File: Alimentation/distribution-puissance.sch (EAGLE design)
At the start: 18 parts

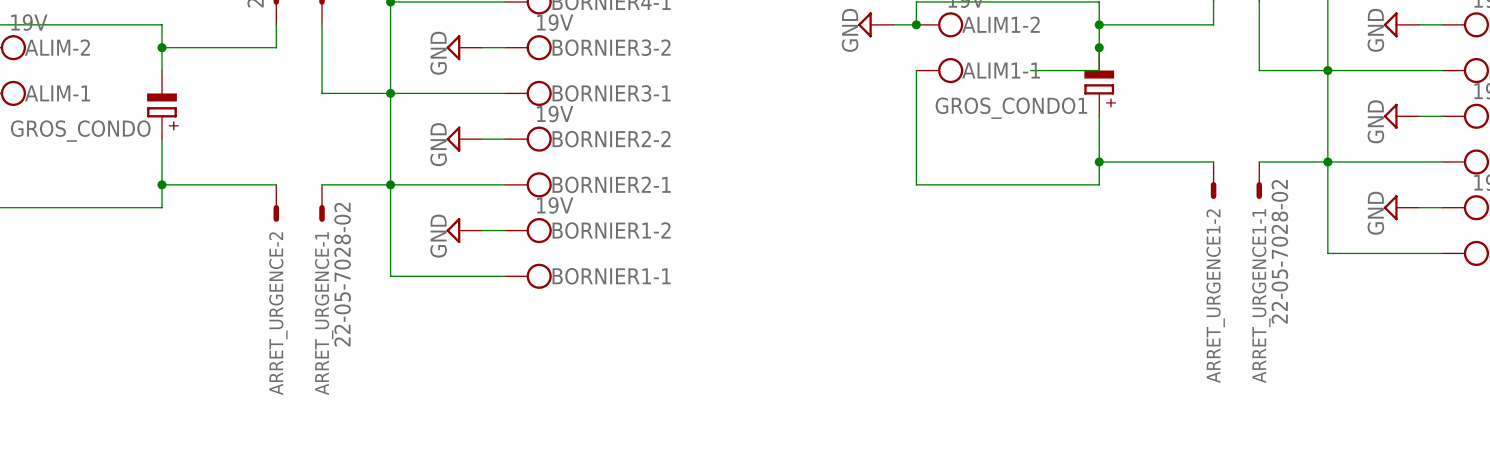
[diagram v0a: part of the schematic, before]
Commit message: utilisation de bornier pour les ARU + plus grosses pistes dans le routage + gerber files
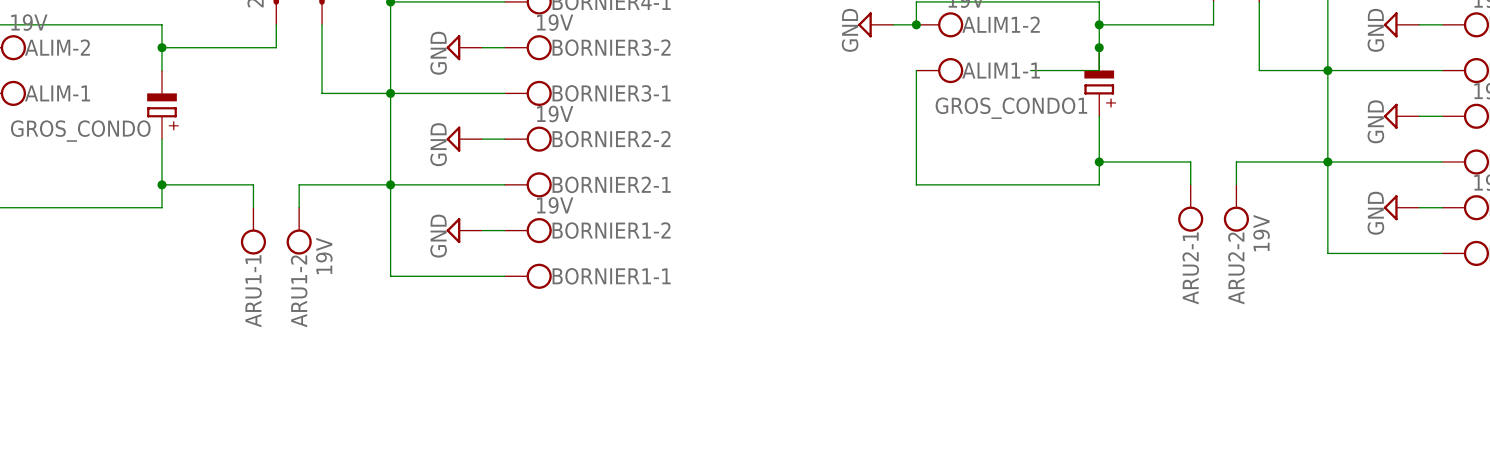
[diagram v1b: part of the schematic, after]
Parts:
- removed ARRET_URGENCE, ARRET_URGENCE1: 22-05-7028-02, con-molex:22-05-7028-02
- added ARU1, ARU2: 19V, con-wago-500:W237-102
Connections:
- net N$1: now also ARU1-2.KL; no longer ARRET_URGENCE-1.S
- net N$2: now also ARU2-2.KL; no longer ARRET_URGENCE1-1.S
- net N$3: now also ARU1-1.KL; no longer ARRET_URGENCE-2.S
- net N$4: now also ARU2-1.KL; no longer ARRET_URGENCE1-2.S
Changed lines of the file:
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@@
 <part name="FRAME1" library="frames" library_urn="urn:adsk.eagle:library:229" deviceset="A4L-LOC" device=""/>
 <part name="GROS_CONDO" library="rcl" library_urn="urn:adsk.eagle:library:334" deviceset="CPOL-EU" device="E10-22.5"/>
-<part name="ARRET_URGENCE" library="con-molex" library_urn="urn:adsk.eagle:library:165" deviceset="22-?-02" device="05-7028"/>
 <part name="VOLTMETRE" library="con-molex" library_urn="urn:adsk.eagle:library:165" deviceset="22-?-02" device="05-7028"/>
 <part name="BORNIER1" library="con-wago-500" library_urn="urn:adsk.eagle:library:195" deviceset="W237-102" device="" value="19V"/>
@@
 <part name="BATTERIE_GND6" library="supply2" library_urn="urn:adsk.eagle:library:372" deviceset="GND" device=""/>
 <part name="GROS_CONDO1" library="rcl" library_urn="urn:adsk.eagle:library:334" deviceset="CPOL-EU" device="E10-22.5"/>
-<part name="ARRET_URGENCE1" library="con-molex" library_urn="urn:adsk.eagle:library:165" deviceset="22-?-02" device="05-7028"/>
 <part name="VOLTMETRE1" library="con-molex" library_urn="urn:adsk.eagle:library:165" deviceset="22-?-02" device="05-7028"/>
 <part name="BORNIER6" library="con-wago-500" library_urn="urn:adsk.eagle:library:195" deviceset="W237-102" device="" value="19V"/>
@@
 <part name="ALIM1" library="con-wago-500" library_urn="urn:adsk.eagle:library:195" deviceset="W237-102" device="" value="19V"/>
 <part name="BATTERIE_GND12" library="supply2" library_urn="urn:adsk.eagle:library:372" deviceset="GND" device=""/>
+<part name="ARU1" library="con-wago-500" library_urn="urn:adsk.eagle:library:195" deviceset="W237-102" device="" value="19V"/>
+<part name="ARU2" library="con-wago-500" library_urn="urn:adsk.eagle:library:195" deviceset="W237-102" device="" value="19V"/>
 </parts>
 <sheets>
@@
 <instance part="FRAME1" gate="G$1" x="0" y="0"/>
 <instance part="GROS_CONDO" gate="G$1" x="35.56" y="88.9" rot="R180"/>
-<instance part="ARRET_URGENCE" gate="-1" x="53.34" y="78.74" rot="R270"/>
-<instance part="ARRET_URGENCE" gate="-2" x="48.26" y="78.74" rot="R270"/>
 <instance part="VOLTMETRE" gate="-1" x="48.26" y="101.6" rot="R90"/>
 <instance part="VOLTMETRE" gate="-2" x="53.34" y="101.6" rot="R90"/>
@@
 <instance part="BATTERIE_GND6" gate="GND" x="10.16" y="96.52" rot="R270"/>
 <instance part="GROS_CONDO1" gate="G$1" x="139.7" y="91.44" rot="R180"/>
-<instance part="ARRET_URGENCE1" gate="-1" x="157.48" y="81.28" rot="R270"/>
-<instance part="ARRET_URGENCE1" gate="-2" x="152.4" y="81.28" rot="R270"/>
 <instance part="VOLTMETRE1" gate="-1" x="152.4" y="104.14" rot="R90"/>
 <instance part="VOLTMETRE1" gate="-2" x="157.48" y="104.14" rot="R90"/>
@@
 <instance part="ALIM1" gate="-2" x="124.46" y="99.06" rot="R180"/>
 <instance part="BATTERIE_GND12" gate="GND" x="114.3" y="99.06" rot="R270"/>
+<instance part="ARU1" gate="-1" x="45.72" y="73.66" rot="R90"/>
+<instance part="ARU1" gate="-2" x="50.8" y="73.66" rot="R90"/>
+<instance part="ARU2" gate="-1" x="149.86" y="76.2" rot="R90"/>
+<instance part="ARU2" gate="-2" x="154.94" y="76.2" rot="R90"/>
 </instances>
 <busses>
@@
 <net name="N$1" class="0">
 <segment>
-<pinref part="ARRET_URGENCE" gate="-1" pin="S"/>
-<wire x1="53.34" y1="81.28" x2="60.96" y2="81.28" width="0.1524" layer="91"/>
 <wire x1="60.96" y1="81.28" x2="60.96" y2="71.12" width="0.1524" layer="91"/>
 <pinref part="BORNIER1" gate="-1" pin="KL"/>
@@
 <wire x1="53.34" y1="99.06" x2="53.34" y2="91.44" width="0.1524" layer="91"/>
 <wire x1="53.34" y1="91.44" x2="60.96" y2="91.44" width="0.1524" layer="91"/>
+<pinref part="ARU1" gate="-2" pin="KL"/>
+<wire x1="50.8" y1="78.74" x2="50.8" y2="81.28" width="0.1524" layer="91"/>
+<wire x1="50.8" y1="81.28" x2="60.96" y2="81.28" width="0.1524" layer="91"/>
 </segment>
 </net>
 <net name="N$2" class="0">
 <segment>
-<pinref part="ARRET_URGENCE1" gate="-1" pin="S"/>
-<wire x1="157.48" y1="83.82" x2="165.1" y2="83.82" width="0.1524" layer="91"/>
 <wire x1="165.1" y1="83.82" x2="165.1" y2="73.66" width="0.1524" layer="91"/>
 <pinref part="BORNIER6" gate="-1" pin="KL"/>
@@
 <wire x1="157.48" y1="101.6" x2="157.48" y2="93.98" width="0.1524" layer="91"/>
 <wire x1="157.48" y1="93.98" x2="165.1" y2="93.98" width="0.1524" layer="91"/>
+<pinref part="ARU2" gate="-2" pin="KL"/>
+<wire x1="154.94" y1="81.28" x2="154.94" y2="83.82" width="0.1524" layer="91"/>
+<wire x1="154.94" y1="83.82" x2="165.1" y2="83.82" width="0.1524" layer="91"/>
 </segment>
 </net>
@@
 <pinref part="GROS_CONDO" gate="G$1" pin="+"/>
 <wire x1="35.56" y1="86.36" x2="35.56" y2="81.28" width="0.1524" layer="91"/>
-<pinref part="ARRET_URGENCE" gate="-2" pin="S"/>
-<wire x1="48.26" y1="81.28" x2="35.56" y2="81.28" width="0.1524" layer="91"/>
 <wire x1="35.56" y1="81.28" x2="35.56" y2="78.74" width="0.1524" layer="91"/>
-<junction x="35.56" y="81.28"/>
 <wire x1="35.56" y1="78.74" x2="15.24" y2="78.74" width="0.1524" layer="91"/>
 <wire x1="15.24" y1="78.74" x2="15.24" y2="91.44" width="0.1524" layer="91"/>
+<pinref part="ARU1" gate="-1" pin="KL"/>
+<wire x1="45.72" y1="78.74" x2="45.72" y2="81.28" width="0.1524" layer="91"/>
+<wire x1="45.72" y1="81.28" x2="35.56" y2="81.28" width="0.1524" layer="91"/>
+<junction x="35.56" y="81.28"/>
 </segment>
 </net>
@@
 <pinref part="GROS_CONDO1" gate="G$1" pin="+"/>
 <wire x1="139.7" y1="88.9" x2="139.7" y2="83.82" width="0.1524" layer="91"/>
-<pinref part="ARRET_URGENCE1" gate="-2" pin="S"/>
-<wire x1="152.4" y1="83.82" x2="139.7" y2="83.82" width="0.1524" layer="91"/>
 <wire x1="139.7" y1="83.82" x2="139.7" y2="81.28" width="0.1524" layer="91"/>
-<junction x="139.7" y="83.82"/>
 <wire x1="139.7" y1="81.28" x2="119.38" y2="81.28" width="0.1524" layer="91"/>
 <wire x1="119.38" y1="81.28" x2="119.38" y2="93.98" width="0.1524" layer="91"/>
-</segment>
-</net>
+<pinref part="ARU2" gate="-1" pin="KL"/>
+<wire x1="149.86" y1="81.28" x2="149.86" y2="83.82" width="0.1524" layer="91"/>
+<wire x1="149.86" y1="83.82" x2="139.7" y2="83.82" width="0.1524" layer="91"/>
+<junction x="139.7" y="83.82"/>
+</segment>
+</net>

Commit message: carte puissance v2
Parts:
- removed ARU1, ARU2, BORNIER10, BORNIER6, BORNIER7, BORNIER8, BORNIER9: 19V, con-wago-500:W237-102
- added ARU-LOGIQUE, INTERUPTEUR-LOGIQUE: 5V, con-wago-500:W237-102
- added ARU-PUISSANCE, INTERUPTEUR-PUISSANCE: 19V, con-wago-500:W237-102
- added LOGIQUE1, LOGIQUE2, LOGIQUE3, LOGIQUE4, LOGIQUE5: 22-05-7028-02, con-molex:22-05-7028-02
- ALIM-LOGIQUE: value 19V -> 5V
- renumbered ALIM to ALIM-PUISSANCE, ALIM1 to ALIM-LOGIQUE, BORNIER1 to PUISSANCE1, BORNIER2 to PUISSANCE2, BORNIER3 to PUISSANCE3, BORNIER4 to PUISSANCE4, BORNIER5 to PUISSANCE5
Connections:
- new net N$5: ARU-PUISSANCE-2.KL, INTERUPTEUR-PUISSANCE-1.KL
- new net N$6: ARU-LOGIQUE-2.KL, INTERUPTEUR-LOGIQUE-1.KL
- net GND: now also LOGIQUE1-1.S, LOGIQUE2-1.S, LOGIQUE3-1.S, LOGIQUE4-1.S, LOGIQUE5-1.S; no longer BORNIER10-2.KL, BORNIER6-2.KL, BORNIER7-2.KL, BORNIER8-2.KL, BORNIER9-2.KL
- net N$1: now also INTERUPTEUR-PUISSANCE-2.KL; no longer ARU1-2.KL
- net N$2: now also INTERUPTEUR-LOGIQUE-2.KL, LOGIQUE1-2.S, LOGIQUE2-2.S, LOGIQUE3-2.S, LOGIQUE4-2.S, LOGIQUE5-2.S; no longer ARU2-2.KL, BORNIER10-1.KL, BORNIER6-1.KL, BORNIER7-1.KL, BORNIER8-1.KL, BORNIER9-1.KL
- net N$3: now also ARU-PUISSANCE-1.KL; no longer ARU1-1.KL
- net N$4: now also ARU-LOGIQUE-1.KL; no longer ARU2-1.KL
